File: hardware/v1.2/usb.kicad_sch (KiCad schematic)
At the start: 43 parts, among them J3 USB_C_Receptacle_USB2.0_14P, J4 USB_C_Receptacle_USB2.0_14P, J5 USB_C_Receptacle_USB2.0_14P, U1 ECP5U_25F_CABGA256, U6 FT231XQ, U7 TPD2EUSB30A, U8 TPD2EUSB30A, U9 TPD2EUSB30A

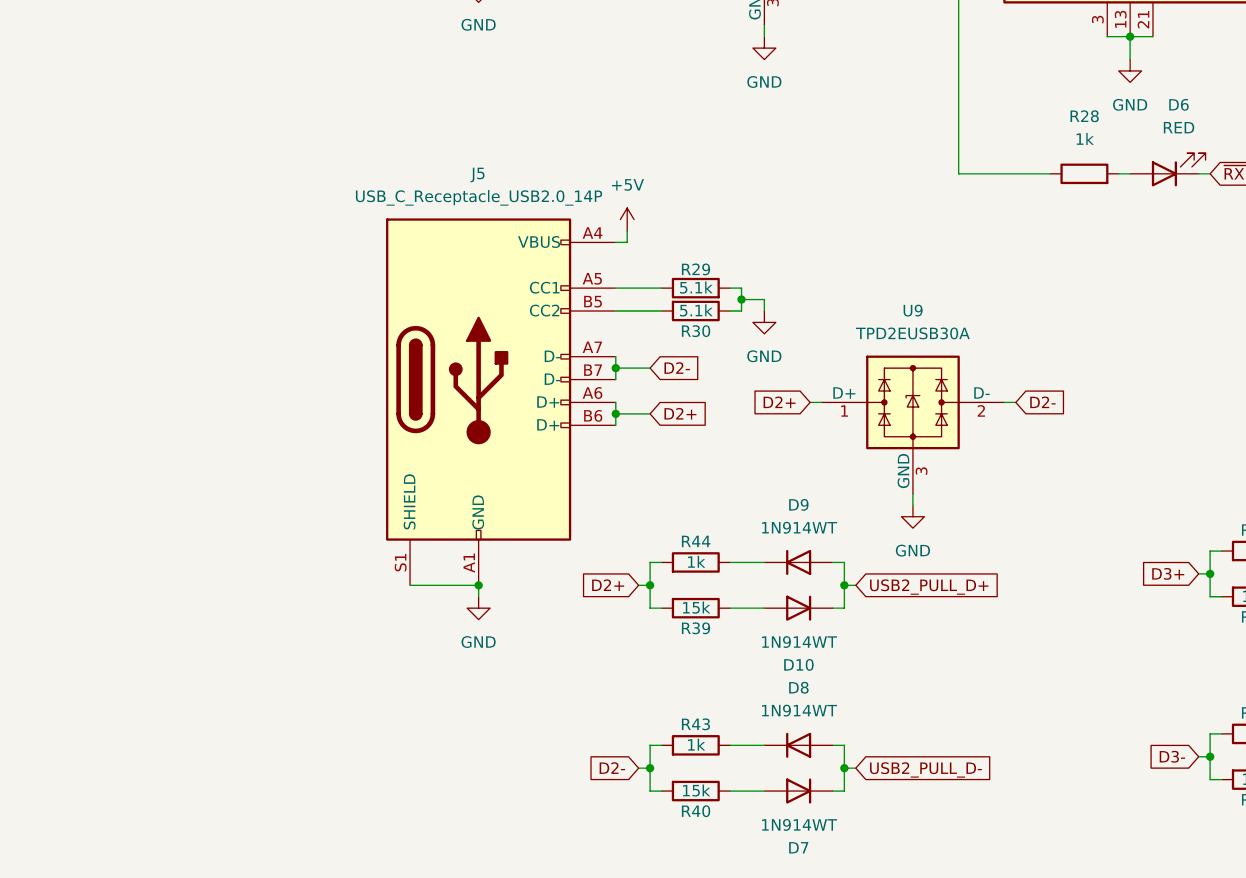
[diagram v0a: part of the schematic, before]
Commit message: Update pic on readme
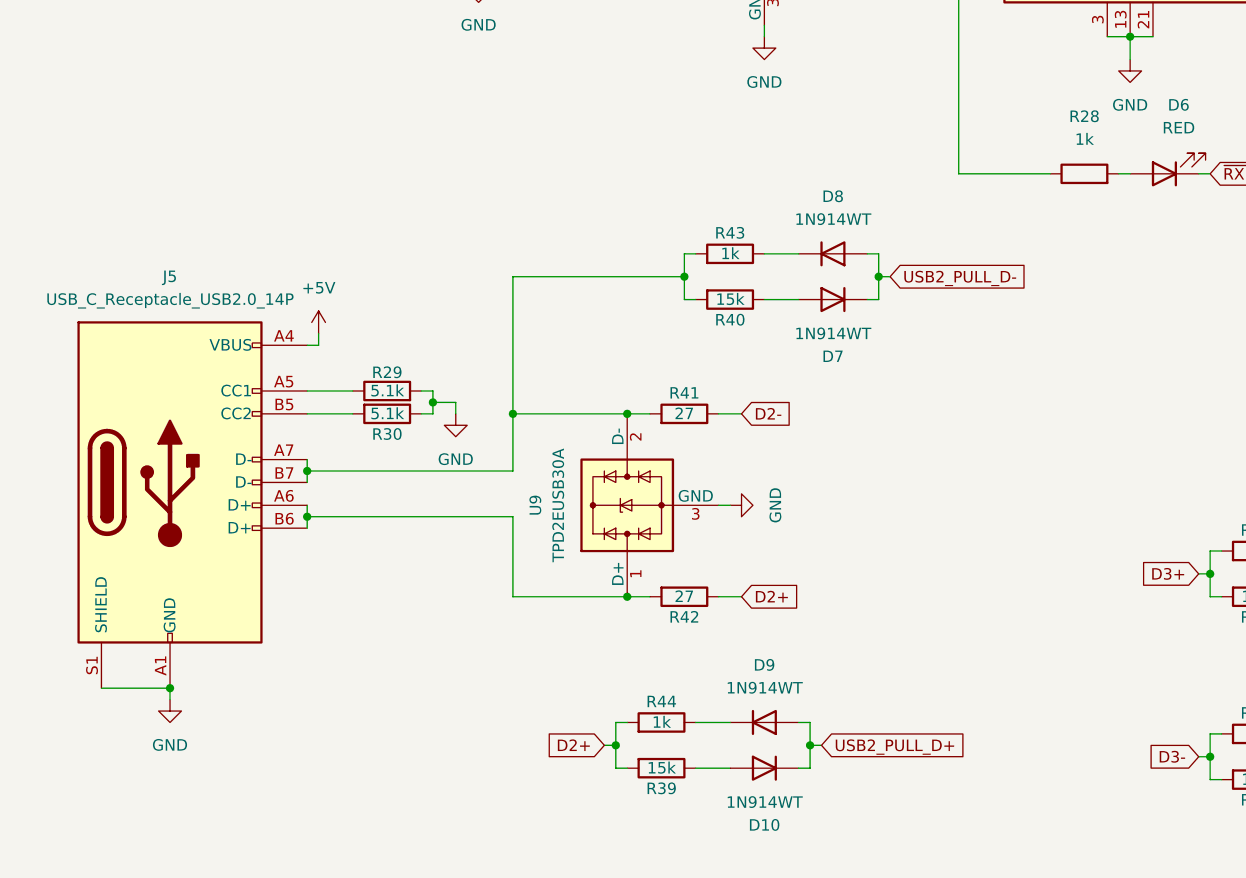
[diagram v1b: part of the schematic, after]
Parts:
- added R41, R42: 27, Resistor_SMD:R_0201_0603Metric, symbol Device:R
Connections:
- net D2+: now also R42.1; no longer J5.A6 (D+), J5.B6 (D+), U9.1 (D+)
- net D2-: now also R41.1; no longer J5.A7 (D-), J5.B7 (D-), R40.2, R43.2, U9.2 (D-)
- new net: J5.A7 (D-), J5.B7 (D-), R40.2, R41.2, R43.2, U9.2 (D-)
- new net: J5.A6 (D+), J5.B6 (D+), R42.2, U9.1 (D+)
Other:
- moved on the sheet: D10, D7, D8, D9, J5, R29, R30, R39, R40, R43, R44, U9

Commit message: Trying to document my journey :)
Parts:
- added R30, R33: 27, Resistor_SMD:R_0201_0603Metric, symbol Device:R
- renumbered D7 to D10, D9 to D13, D10 to D14, D13 to D6, D14 to D7, D6 to D8, D8 to D9, R22 to R20, R23 to R21, R24 to R22, R25 to R23, R20 to R24, R21 to R25, R47 to R26, R48 to R27, R26 to R29, R27 to R31, R43 to R32, R40 to R34, R45 to R35, R29 to R36, R30 to R37, R41 to R38, R46 to R39, R42 to R40, R44 to R41, R39 to R42
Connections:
- net D3+: now also R33.1; no longer J4.A6 (D+), J4.B6 (D+), R35.2, R39.2, U8.1 (D+)
- net D3-: now also R30.1; no longer J4.A7 (D-), J4.B7 (D-), R26.2, R27.2, U8.2 (D-)
- net D2A-: now reaches J5.A7 (D-), J5.B7 (D-), R32.2, R34.2, R38.2, U9.2 (D-)
- net D2A+: now reaches J5.A6 (D+), J5.B6 (D+), R40.2, U9.1 (D+)
- new net D3A+: J4.A6 (D+), J4.B6 (D+), R33.2, R35.2, R39.2, U8.1 (D+)
- new net D3A-: J4.A7 (D-), J4.B7 (D-), R26.2, R27.2, R30.2, U8.2 (D-)
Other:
- moved on the sheet: C38, D10, D11, D12, D13, D14, D6, D7, D8, D9, J3, J5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
